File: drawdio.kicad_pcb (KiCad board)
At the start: 2 copper layers, 45.7 x 12.7 mm, 12 parts, among them P1 CONN_2, P2 CONN_01X01, Q1 BC558, Q2 BC547, U1 LM555N

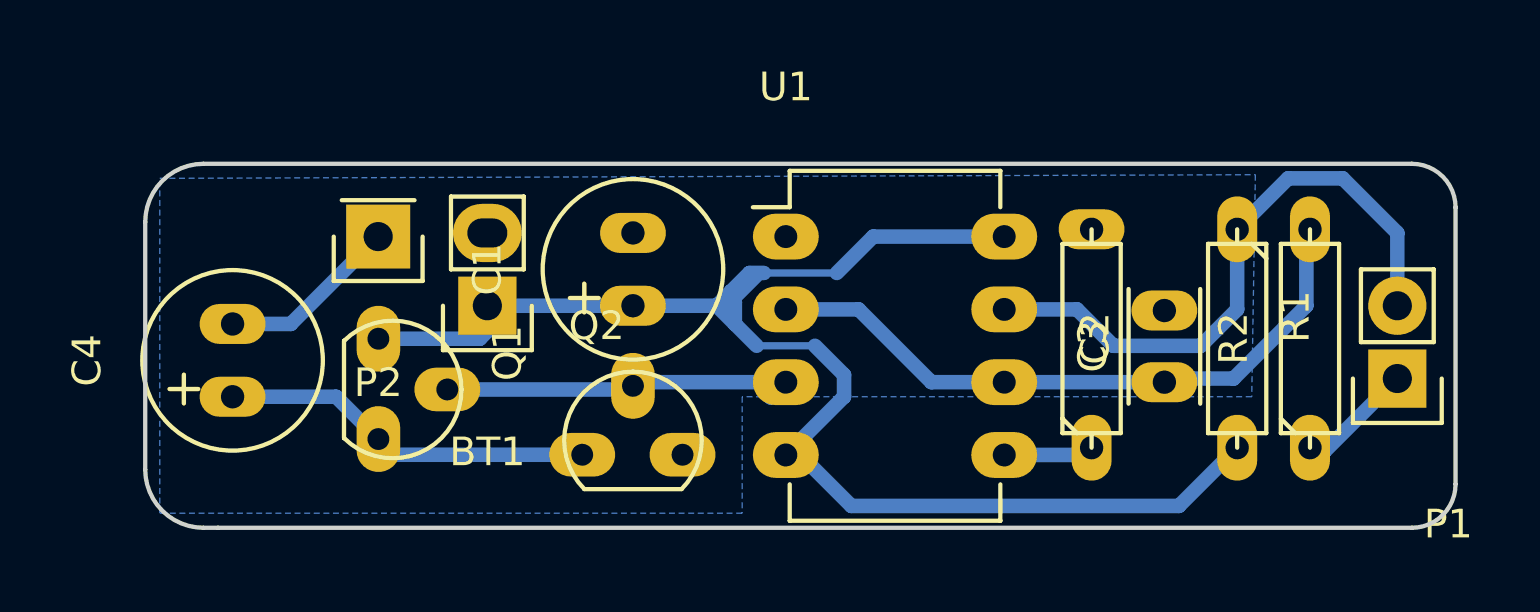
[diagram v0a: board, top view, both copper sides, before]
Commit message: Add GND plane in front layer
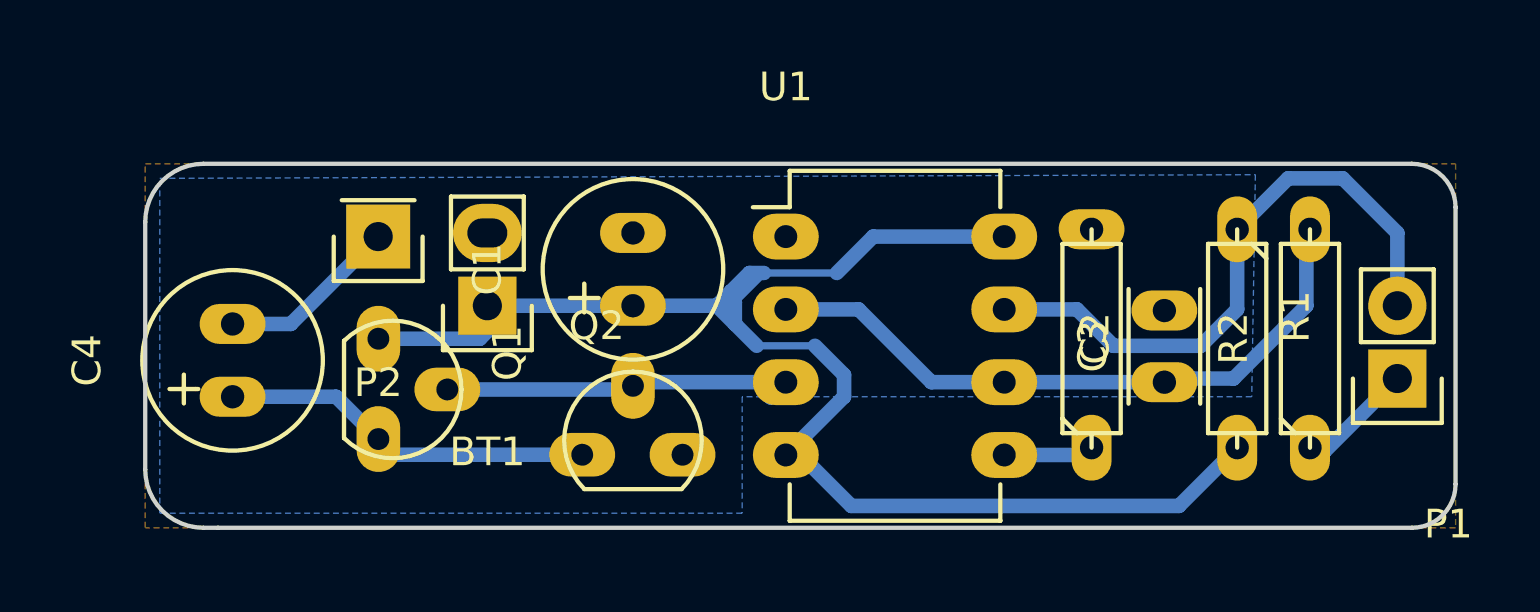
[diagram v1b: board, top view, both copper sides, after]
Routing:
- added copper zone on F.Cu, net GND
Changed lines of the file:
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@@
+    )
+  )
+  (zone (net 1) (net_name GND) (layer F.Cu) (hatch edge 0.508)
+    (connect_pads (clearance 0.508))
+    (min_thickness 0.254)
+    (fill yes (arc_segments 16) (thermal_gap 0.508) (thermal_bridge_width 0.508))
+    (polygon
+      (pts
+        (xy 126.492 93.472) (xy 80.772 93.472) (xy 80.772 80.772) (xy 126.492 80.772) (xy 126.492 93.472)
+      )
     )
   )
